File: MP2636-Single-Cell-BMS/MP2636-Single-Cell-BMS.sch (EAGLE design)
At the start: 15 parts, among them U1 MP2636GR-P

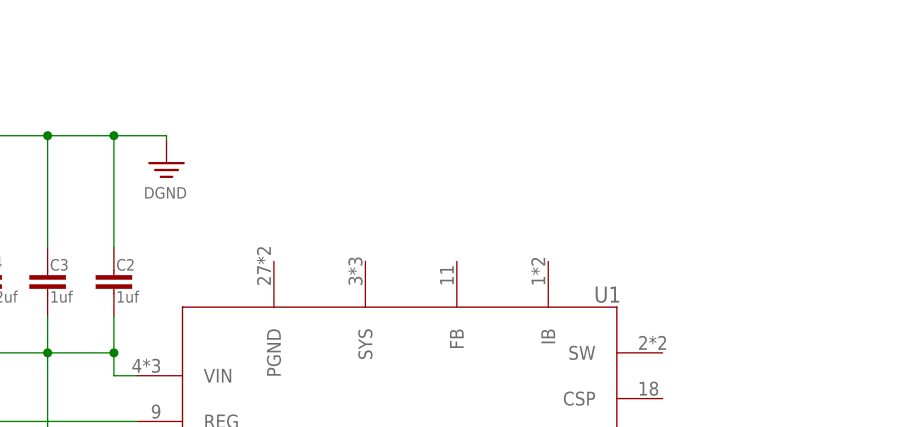
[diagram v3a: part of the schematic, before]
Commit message: Output circuit is added
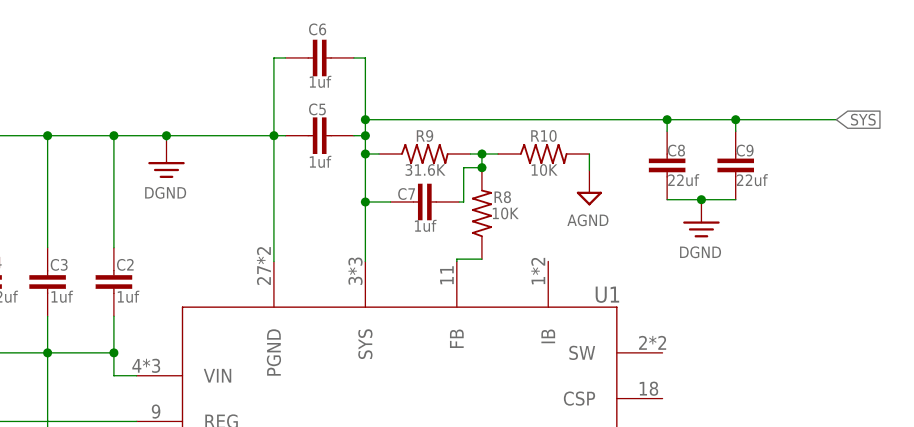
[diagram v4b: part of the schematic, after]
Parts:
- added C5, C6, C7: 1uf, Capacitor:C_CHIP-0805(2012-METRIC)
- added C8, C9: 22uf, Capacitor:C_CHIP-0805(2012-METRIC)
- added R10, R8: 10K, Resistor:R-US_CHIP-0805(2012-METRIC)
- added R9: 31.6K, Resistor:R-US_CHIP-0805(2012-METRIC)
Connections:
- new net N$10: C7.2, R10.1, R8.2, R9.2
- new net N$9: R8.1, U1.FB
- new net SYS: C5.2, C6.2, C7.1, C8.2, C9.2, R9.1, U1.SYS
- net AGND: now also R10.2
- net DGND: now also C5.1, C6.1, C8.1, C9.1, U1.PGND
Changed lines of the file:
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@@
 <part name="C4" library="Capacitor" deviceset="C" device="CHIP-0805(2012-METRIC)" package3d_urn="urn:adsk.eagle:package:16290897/2" technology="_" value="22uf"/>
 <part name="SUPPLY4" library="Power_Symbols" deviceset="DGND-EARTH" device="" value="DGND"/>
+<part name="C5" library="Capacitor" deviceset="C" device="CHIP-0805(2012-METRIC)" package3d_urn="urn:adsk.eagle:package:16290897/2" technology="_" value="1uf"/>
+<part name="C6" library="Capacitor" deviceset="C" device="CHIP-0805(2012-METRIC)" package3d_urn="urn:adsk.eagle:package:16290897/2" technology="_" value="1uf"/>
+<part name="C7" library="Capacitor" deviceset="C" device="CHIP-0805(2012-METRIC)" package3d_urn="urn:adsk.eagle:package:16290897/2" technology="_" value="1uf"/>
+<part name="R8" library="Resistor" deviceset="R-US" device="CHIP-0805(2012-METRIC)" package3d_urn="urn:adsk.eagle:package:16378559/2" technology="_" value="10K"/>
+<part name="R9" library="Resistor" deviceset="R-US" device="CHIP-0805(2012-METRIC)" package3d_urn="urn:adsk.eagle:package:16378559/2" technology="_" value="31.6K"/>
+<part name="R10" library="Resistor" deviceset="R-US" device="CHIP-0805(2012-METRIC)" package3d_urn="urn:adsk.eagle:package:16378559/2" technology="_" value="10K"/>
+<part name="C8" library="Capacitor" deviceset="C" device="CHIP-0805(2012-METRIC)" package3d_urn="urn:adsk.eagle:package:16290897/2" technology="_" value="22uf"/>
+<part name="C9" library="Capacitor" deviceset="C" device="CHIP-0805(2012-METRIC)" package3d_urn="urn:adsk.eagle:package:16290897/2" technology="_" value="22uf"/>
+<part name="SUPPLY5" library="Power_Symbols" deviceset="AGND" device="" value="AGND"/>
+<part name="SUPPLY6" library="Power_Symbols" deviceset="DGND-EARTH" device="" value="DGND"/>
 </parts>
 <sheets>
@@
 <instance part="SUPPLY4" gate="G$1" x="104.902" y="137.922" smashed="yes">
 <attribute name="VALUE" x="104.775" y="133.985" size="1.27" layer="96" align="bottom-center"/>
+</instance>
+<instance part="C5" gate="G$1" x="120.65" y="140.97" smashed="yes" rot="R90">
+<attribute name="NAME" x="120.65" y="143.256" size="1.27" layer="95"/>
+<attribute name="VALUE" x="120.65" y="137.414" size="1.27" layer="96"/>
+</instance>
+<instance part="C6" gate="G$1" x="120.65" y="149.606" smashed="yes" rot="R90">
+<attribute name="NAME" x="120.65" y="152.146" size="1.27" layer="95"/>
+<attribute name="VALUE" x="120.65" y="146.304" size="1.27" layer="96"/>
+</instance>
+<instance part="C7" gate="G$1" x="132.334" y="133.604" smashed="yes" rot="R90">
+<attribute name="NAME" x="130.556" y="133.858" size="1.27" layer="95"/>
+<attribute name="VALUE" x="132.334" y="130.302" size="1.27" layer="96"/>
+</instance>
+<instance part="R8" gate="G$1" x="139.954" y="132.334" smashed="yes" rot="R90">
+<attribute name="NAME" x="142.24" y="134.1374" size="1.27" layer="95" rot="R180" align="center"/>
+<attribute name="VALUE" x="142.494" y="132.334" size="1.27" layer="96" rot="R180" align="center"/>
+</instance>
+<instance part="R9" gate="G$1" x="133.604" y="138.938" smashed="yes">
+<attribute name="NAME" x="133.604" y="140.9446" size="1.27" layer="95" align="center"/>
+<attribute name="VALUE" x="133.604" y="137.16" size="1.27" layer="96" align="center"/>
+</instance>
+<instance part="R10" gate="G$1" x="146.812" y="138.938" smashed="yes">
+<attribute name="NAME" x="146.812" y="140.9446" size="1.27" layer="95" align="center"/>
+<attribute name="VALUE" x="146.812" y="137.16" size="1.27" layer="96" align="center"/>
+</instance>
+<instance part="C8" gate="G$1" x="160.528" y="136.398" smashed="yes" rot="R180">
+<attribute name="NAME" x="160.528" y="138.684" size="1.27" layer="95"/>
+<attribute name="VALUE" x="160.528" y="135.382" size="1.27" layer="96"/>
+</instance>
+<instance part="C9" gate="G$1" x="168.148" y="136.398" smashed="yes" rot="R180">
+<attribute name="NAME" x="168.148" y="138.684" size="1.27" layer="95"/>
+<attribute name="VALUE" x="168.148" y="135.382" size="1.27" layer="96"/>
+</instance>
+<instance part="SUPPLY5" gate="G$1" x="151.892" y="134.62" smashed="yes">
+<attribute name="VALUE" x="151.765" y="130.937" size="1.27" layer="96" align="bottom-center"/>
+</instance>
+<instance part="SUPPLY6" gate="G$1" x="164.338" y="131.318" smashed="yes">
+<attribute name="VALUE" x="164.211" y="127.381" size="1.27" layer="96" align="bottom-center"/>
 </instance>
 </instances>
@@
 <pinref part="SUPPLY4" gate="G$1" pin="DGND"/>
 <wire x1="99.06" y1="140.97" x2="104.902" y2="140.97" width="0.1524" layer="91"/>
-<wire x1="104.902" y1="140.97" x2="104.902" y2="140.462" width="0.1524" layer="91"/>
+<wire x1="104.902" y1="140.462" x2="104.902" y2="140.97" width="0.1524" layer="91"/>
+<junction x="104.902" y="140.97"/>
+<pinref part="C5" gate="G$1" pin="1"/>
+<wire x1="104.902" y1="140.97" x2="116.84" y2="140.97" width="0.1524" layer="91"/>
+<pinref part="U1" gate="G$1" pin="PGND"/>
+<wire x1="116.84" y1="127" x2="116.84" y2="140.97" width="0.1524" layer="91"/>
+<wire x1="116.84" y1="140.97" x2="118.11" y2="140.97" width="0.1524" layer="91"/>
+<wire x1="116.84" y1="140.97" x2="116.84" y2="149.606" width="0.1524" layer="91"/>
+<junction x="116.84" y="140.97"/>
+<pinref part="C6" gate="G$1" pin="1"/>
+<wire x1="116.84" y1="149.606" x2="118.11" y2="149.606" width="0.1524" layer="91"/>
+</segment>
+<segment>
+<pinref part="C8" gate="G$1" pin="1"/>
+<pinref part="C9" gate="G$1" pin="1"/>
+<wire x1="160.528" y1="133.858" x2="164.338" y2="133.858" width="0.1524" layer="91"/>
+<pinref part="SUPPLY6" gate="G$1" pin="DGND"/>
+<wire x1="164.338" y1="133.858" x2="168.148" y2="133.858" width="0.1524" layer="91"/>
+<junction x="164.338" y="133.858"/>
 </segment>
 </net>
@@
 <junction x="53.086" y="111.506"/>
 </segment>
-</net>
+<segment>
+<pinref part="R10" gate="G$1" pin="2"/>
+<pinref part="SUPPLY5" gate="G$1" pin="AGND"/>
+<wire x1="151.892" y1="138.938" x2="151.892" y2="137.16" width="0.1524" layer="91"/>
+</segment>
+</net>
+<net name="SYS" class="0">
+<segment>
+<pinref part="U1" gate="G$1" pin="SYS"/>
+<pinref part="C5" gate="G$1" pin="2"/>
+<wire x1="127" y1="127" x2="127" y2="133.604" width="0.1524" layer="91"/>
+<wire x1="127" y1="133.604" x2="127" y2="138.938" width="0.1524" layer="91"/>
+<wire x1="127" y1="138.938" x2="127" y2="140.97" width="0.1524" layer="91"/>
+<wire x1="127" y1="140.97" x2="125.73" y2="140.97" width="0.1524" layer="91"/>
+<pinref part="C6" gate="G$1" pin="2"/>
+<wire x1="125.73" y1="149.606" x2="127" y2="149.606" width="0.1524" layer="91"/>
+<wire x1="127" y1="149.606" x2="127" y2="142.748" width="0.1524" layer="91"/>
+<junction x="127" y="140.97"/>
+<pinref part="R9" gate="G$1" pin="1"/>
+<wire x1="127" y1="142.748" x2="127" y2="140.97" width="0.1524" layer="91"/>
+<wire x1="128.524" y1="138.938" x2="127" y2="138.938" width="0.1524" layer="91"/>
+<junction x="127" y="138.938"/>
+<pinref part="C7" gate="G$1" pin="1"/>
+<wire x1="129.794" y1="133.604" x2="127" y2="133.604" width="0.1524" layer="91"/>
+<junction x="127" y="133.604"/>
+<wire x1="127" y1="142.748" x2="160.528" y2="142.748" width="0.1524" layer="91"/>
+<junction x="127" y="142.748"/>
+<pinref part="C8" gate="G$1" pin="2"/>
+<wire x1="160.528" y1="142.748" x2="168.148" y2="142.748" width="0.1524" layer="91"/>
+<wire x1="160.528" y1="141.478" x2="160.528" y2="142.748" width="0.1524" layer="91"/>
+<junction x="160.528" y="142.748"/>
+<pinref part="C9" gate="G$1" pin="2"/>
+<wire x1="168.148" y1="141.478" x2="168.148" y2="142.748" width="0.1524" layer="91"/>
+<junction x="168.148" y="142.748"/>
+<wire x1="168.148" y1="142.748" x2="179.324" y2="142.748" width="0.1524" layer="91"/>
+<label x="179.324" y="142.748" size="1.27" layer="95" xref="yes"/>
+</segment>
+</net>
+<net name="N$9" class="0">
+<segment>
+<pinref part="U1" gate="G$1" pin="FB"/>
+<pinref part="R8" gate="G$1" pin="1"/>
+<wire x1="137.16" y1="127" x2="137.16" y2="127.254" width="0.1524" layer="91"/>
+<wire x1="137.16" y1="127.254" x2="139.954" y2="127.254" width="0.1524" layer="91"/>
+</segment>
+</net>
+<net name="N$10" class="0">
+<segment>
+<pinref part="R9" gate="G$1" pin="2"/>
+<pinref part="R10" gate="G$1" pin="1"/>
+<wire x1="138.684" y1="138.938" x2="139.954" y2="138.938" width="0.1524" layer="91"/>
+<wire x1="139.954" y1="138.938" x2="141.732" y2="138.938" width="0.1524" layer="91"/>
+<pinref part="R8" gate="G$1" pin="2"/>
+<wire x1="139.954" y1="137.414" x2="139.954" y2="138.938" width="0.1524" layer="91"/>
+<junction x="139.954" y="138.938"/>
+<pinref part="C7" gate="G$1" pin="2"/>
+<wire x1="137.414" y1="133.604" x2="137.922" y2="133.604" width="0.1524" layer="91"/>
+<wire x1="137.922" y1="133.604" x2="137.922" y2="137.414" width="0.1524" layer="91"/>
+<wire x1="137.922" y1="137.414" x2="139.954" y2="137.414" width="0.1524" layer="91"/>
+<junction x="139.954" y="137.414"/>
+</segment>
+</net>

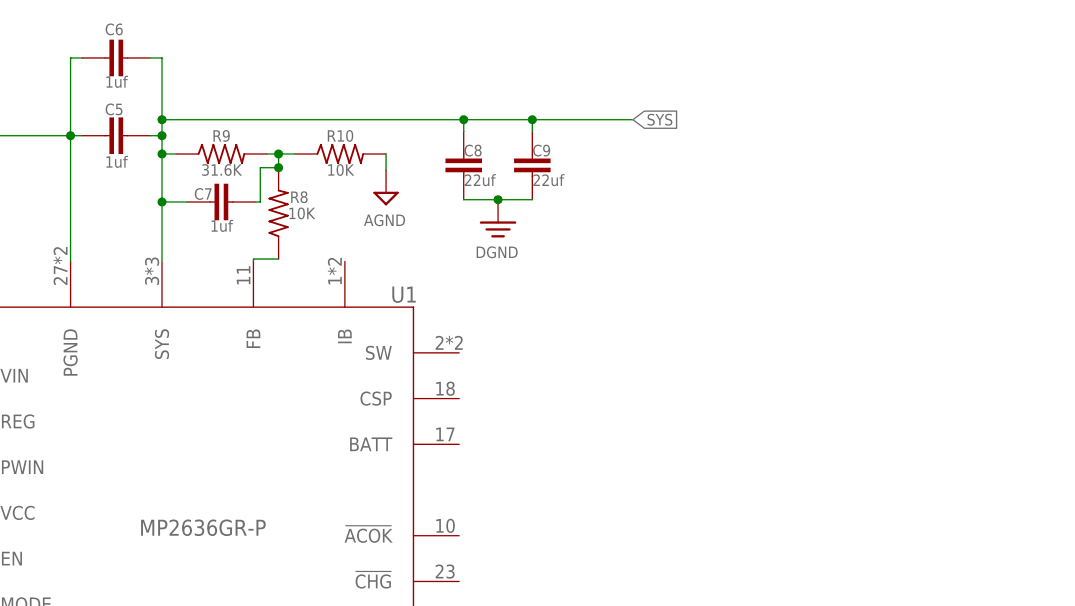
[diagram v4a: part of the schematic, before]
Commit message: Battery circuit is added
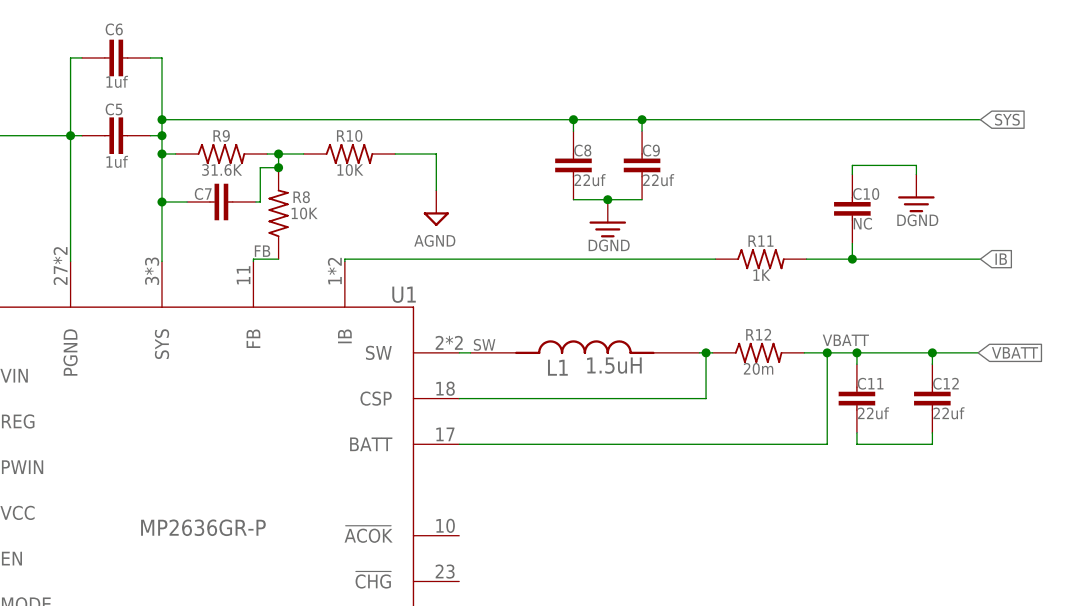
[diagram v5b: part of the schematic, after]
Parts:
- added C10: NC, Capacitor:C_CHIP-0805(2012-METRIC)
- added C11, C12: 22uf, Capacitor:C_CHIP-0805(2012-METRIC)
- added L1: 1.5uH, LQH5BPN2R2NT0L:LQH5BPN2R2NT0L
- added R11: 1K, Resistor:R-US_CHIP-0805(2012-METRIC)
- added R12: 20m, Resistor:R-US_CHIP-0805(2012-METRIC)
- C7: value 1uf -> (none)
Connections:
- net N$9 renamed FB
- new net IB: C10.1, R11.2
- new net N$1: R11.1, U1.IB
- new net N$12: L1.2, R12.1, U1.CSP
- new net N$13: C11.1, C12.1
- new net SW: L1.1, U1.SW
- new net VBATT: C11.2, C12.2, R12.2, U1.BATT
- net DGND: now also C10.2
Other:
- moved on the sheet: C8, C9, R10

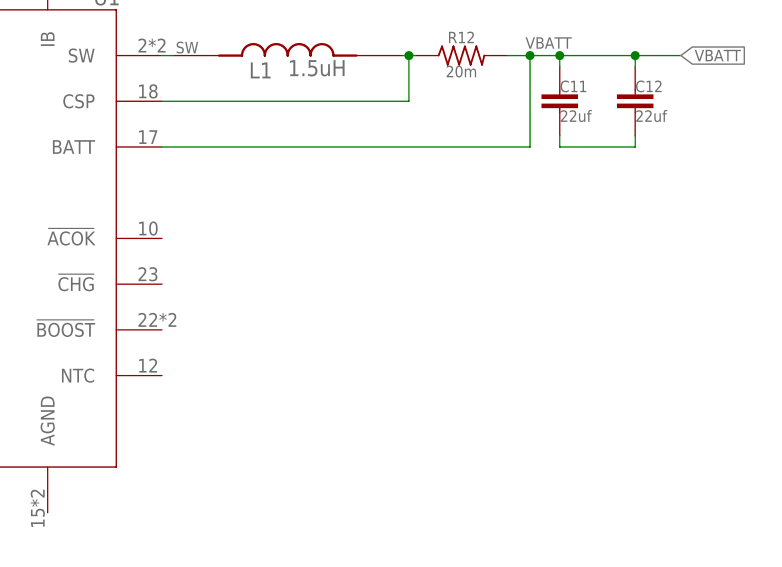
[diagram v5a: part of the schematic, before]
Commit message: Indicator circuit is added
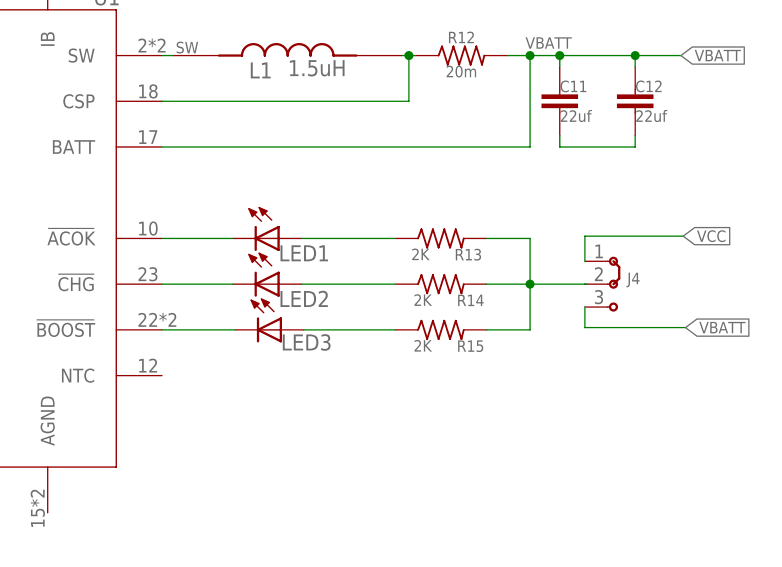
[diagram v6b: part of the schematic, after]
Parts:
- added J4: (no value), jumper:J2X2MM
- added LED1, LED2, LED3: (no value), led:LEDCHIP-LED0805
- added R13, R14, R15: 2K, Resistor:R-US_CHIP-0805(2012-METRIC)
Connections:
- new net N$11: LED2.C, U1.!CHG
- new net N$14: LED3.C, U1.!BOOST
- new net N$15: LED1.A, R13.1
- new net N$16: LED2.A, R14.1
- new net N$17: LED3.A, R15.1
- new net N$18: R13.2, R14.2, R15.2
- new net N$19: J4.2
- new net N$9: LED1.C, U1.!ACOK
- net VBATT: now also J4.3
- net VCC: now also J4.1
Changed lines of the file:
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@@
 <part name="C11" library="Capacitor" deviceset="C" device="CHIP-0805(2012-METRIC)" package3d_urn="urn:adsk.eagle:package:16290897/2" technology="_" value="22uf"/>
 <part name="C12" library="Capacitor" deviceset="C" device="CHIP-0805(2012-METRIC)" package3d_urn="urn:adsk.eagle:package:16290897/2" technology="_" value="22uf"/>
+<part name="LED1" library="led" deviceset="LED" device="CHIP-LED0805"/>
+<part name="LED2" library="led" deviceset="LED" device="CHIP-LED0805"/>
+<part name="LED3" library="led" deviceset="LED" device="CHIP-LED0805"/>
+<part name="R13" library="Resistor" deviceset="R-US" device="CHIP-0805(2012-METRIC)" package3d_urn="urn:adsk.eagle:package:16378559/2" technology="_" value="2K"/>
+<part name="R14" library="Resistor" deviceset="R-US" device="CHIP-0805(2012-METRIC)" package3d_urn="urn:adsk.eagle:package:16378559/2" technology="_" value="2K"/>
+<part name="R15" library="Resistor" deviceset="R-US" device="CHIP-0805(2012-METRIC)" package3d_urn="urn:adsk.eagle:package:16378559/2" technology="_" value="2K"/>
+<part name="J4" library="jumper" deviceset="J2" device="X2MM" package3d_urn="urn:adsk.eagle:package:15506/1"/>
 </parts>
 <sheets>
@@
 <attribute name="NAME" x="212.598" y="112.776" size="1.27" layer="95"/>
 <attribute name="VALUE" x="212.598" y="109.474" size="1.27" layer="96"/>
+</instance>
+<instance part="LED1" gate="G$1" x="172.974" y="96.52" smashed="yes" rot="R270">
+<attribute name="NAME" x="172.974" y="93.98" size="1.778" layer="95"/>
+<attribute name="VALUE" x="168.402" y="90.805" size="1.778" layer="96"/>
+</instance>
+<instance part="LED2" gate="G$1" x="172.974" y="91.44" smashed="yes" rot="R270">
+<attribute name="NAME" x="172.974" y="88.9" size="1.778" layer="95"/>
+<attribute name="VALUE" x="168.402" y="85.725" size="1.778" layer="96"/>
+</instance>
+<instance part="LED3" gate="G$1" x="173.228" y="86.36" smashed="yes" rot="R270">
+<attribute name="NAME" x="173.228" y="84.074" size="1.778" layer="95"/>
+<attribute name="VALUE" x="168.656" y="80.645" size="1.778" layer="96"/>
+</instance>
+<instance part="R13" gate="G$1" x="191.008" y="96.52" smashed="yes">
+<attribute name="NAME" x="194.056" y="94.7166" size="1.27" layer="95" align="center"/>
+<attribute name="VALUE" x="188.722" y="94.742" size="1.27" layer="96" align="center"/>
+</instance>
+<instance part="R14" gate="G$1" x="191.008" y="91.44" smashed="yes">
+<attribute name="NAME" x="194.31" y="89.6366" size="1.27" layer="95" align="center"/>
+<attribute name="VALUE" x="188.976" y="89.662" size="1.27" layer="96" align="center"/>
+</instance>
+<instance part="R15" gate="G$1" x="191.008" y="86.36" smashed="yes">
+<attribute name="NAME" x="194.31" y="84.5566" size="1.27" layer="95" align="center"/>
+<attribute name="VALUE" x="188.976" y="84.582" size="1.27" layer="96" align="center"/>
+</instance>
+<instance part="J4" gate="G$1" x="209.55" y="91.44" smashed="yes">
+<attribute name="NAME" x="211.709" y="91.44" size="1.27" layer="95"/>
+<attribute name="VALUE" x="211.455" y="88.9" size="1.778" layer="96"/>
 </instance>
 </instances>
@@
 <wire x1="35.56" y1="99.06" x2="45.72" y2="99.06" width="0.1524" layer="91"/>
 <label x="35.56" y="99.06" size="1.27" layer="95" rot="R180" xref="yes"/>
+</segment>
+<segment>
+<pinref part="J4" gate="G$1" pin="1"/>
+<wire x1="207.01" y1="93.98" x2="207.01" y2="96.774" width="0.1524" layer="91"/>
+<wire x1="207.01" y1="96.774" x2="217.932" y2="96.774" width="0.1524" layer="91"/>
+<label x="217.932" y="96.774" size="1.27" layer="95" xref="yes"/>
 </segment>
 </net>
@@
 <label x="217.678" y="116.84" size="1.27" layer="95" xref="yes"/>
 </segment>
+<segment>
+<pinref part="J4" gate="G$1" pin="3"/>
+<wire x1="207.01" y1="88.9" x2="207.01" y2="86.614" width="0.1524" layer="91"/>
+<wire x1="207.01" y1="86.614" x2="218.186" y2="86.614" width="0.1524" layer="91"/>
+<label x="218.186" y="86.614" size="1.27" layer="95" xref="yes"/>
+</segment>
 </net>
 <net name="N$13" class="0">
@@
 </segment>
 </net>
+<net name="N$9" class="0">
+<segment>
+<pinref part="U1" gate="G$1" pin="!ACOK"/>
+<pinref part="LED1" gate="G$1" pin="C"/>
+<wire x1="160.02" y1="96.52" x2="167.894" y2="96.52" width="0.1524" layer="91"/>
+</segment>
+</net>
+<net name="N$11" class="0">
+<segment>
+<pinref part="U1" gate="G$1" pin="!CHG"/>
+<pinref part="LED2" gate="G$1" pin="C"/>
+<wire x1="160.02" y1="91.44" x2="167.894" y2="91.44" width="0.1524" layer="91"/>
+</segment>
+</net>
+<net name="N$14" class="0">
+<segment>
+<pinref part="U1" gate="G$1" pin="!BOOST"/>
+<pinref part="LED3" gate="G$1" pin="C"/>
+<wire x1="160.02" y1="86.36" x2="168.148" y2="86.36" width="0.1524" layer="91"/>
+</segment>
+</net>
+<net name="N$15" class="0">
+<segment>
+<pinref part="LED1" gate="G$1" pin="A"/>
+<pinref part="R13" gate="G$1" pin="1"/>
+<wire x1="175.514" y1="96.52" x2="185.928" y2="96.52" width="0.1524" layer="91"/>
+</segment>
+</net>
+<net name="N$16" class="0">
+<segment>
+<pinref part="LED2" gate="G$1" pin="A"/>
+<pinref part="R14" gate="G$1" pin="1"/>
+<wire x1="175.514" y1="91.44" x2="185.928" y2="91.44" width="0.1524" layer="91"/>
+</segment>
+</net>
+<net name="N$17" class="0">
+<segment>
+<pinref part="LED3" gate="G$1" pin="A"/>
+<pinref part="R15" gate="G$1" pin="1"/>
+<wire x1="175.768" y1="86.36" x2="185.928" y2="86.36" width="0.1524" layer="91"/>
+</segment>
+</net>
+<net name="N$18" class="0">
+<segment>
+<pinref part="R13" gate="G$1" pin="2"/>
+<wire x1="196.088" y1="96.52" x2="200.914" y2="96.52" width="0.1524" layer="91"/>
+<wire x1="200.914" y1="96.52" x2="200.914" y2="91.44" width="0.1524" layer="91"/>
+<pinref part="R14" gate="G$1" pin="2"/>
+<wire x1="200.914" y1="91.44" x2="196.088" y2="91.44" width="0.1524" layer="91"/>
+<wire x1="200.914" y1="91.44" x2="200.914" y2="86.36" width="0.1524" layer="91"/>
+<junction x="200.914" y="91.44"/>
+<pinref part="R15" gate="G$1" pin="2"/>
+<wire x1="200.914" y1="86.36" x2="196.088" y2="86.36" width="0.1524" layer="91"/>
+</segment>
+</net>
+<net name="N$19" class="0">
+<segment>
+<pinref part="J4" gate="G$1" pin="2"/>
+<wire x1="201.168" y1="91.44" x2="207.01" y2="91.44" width="0.1524" layer="91"/>
+<wire x1="207.264" y1="91.44" x2="207.01" y2="91.44" width="0.1524" layer="91"/>
+</segment>
+</net>
